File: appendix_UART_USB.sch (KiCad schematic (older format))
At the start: 27 parts, among them J504 USB_C_Receptacle, U502 FT2232D, X501 SG5032CCN-6.000000M-HJGA3

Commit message: fixed missing symbol issue fixed 3vout cap on FTDI
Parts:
- removed D501: USBLC6-2SC6, digikey-footprints:SOT23-6L, symbol dk_TVS-Diodes:USBLC6-2SC6
- added C1: 33n, Capacitors_SMD:C_0603, symbol Device:C
- added U1: USBLC6-2SC6, Package_TO_SOT_SMD:SOT-23-6, symbol Power_Protection:USBLC6-2SC6
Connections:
- net labels added: +3.3V, +5V
- net labels removed: 3.3V
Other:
- moved on the sheet: C501

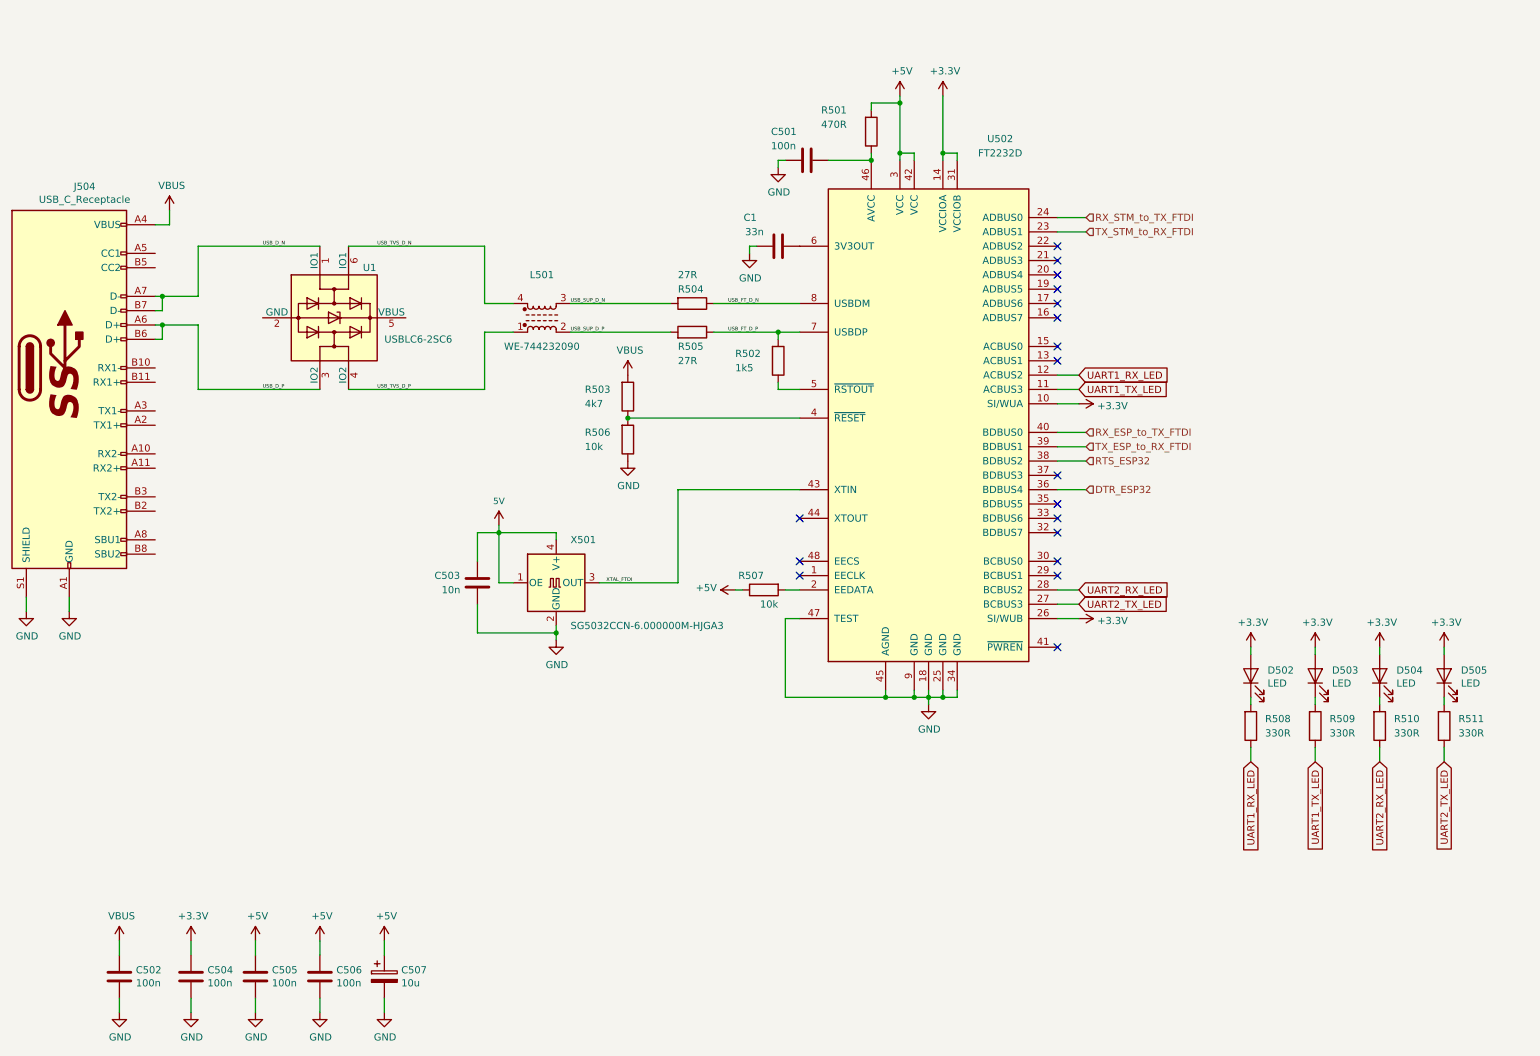
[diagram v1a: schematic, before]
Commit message: started with STM32 Pinout connections (Mittagspause)
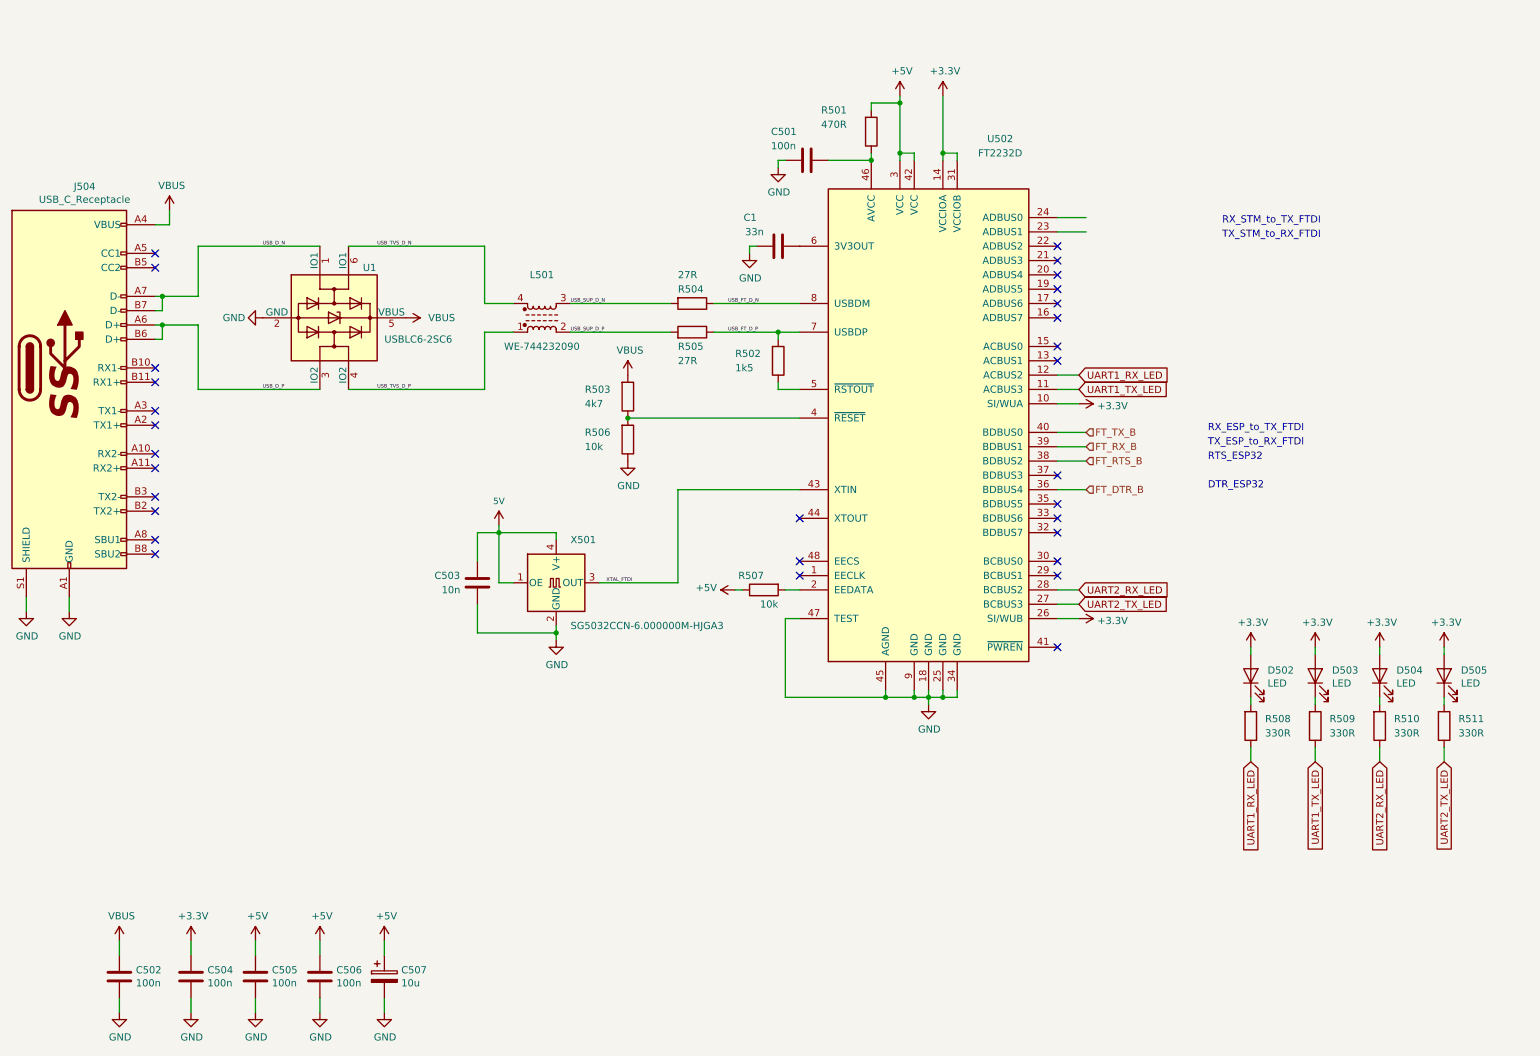
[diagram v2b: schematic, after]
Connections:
- net GND: now also U1.2 (GND)
- net VBUS: now also U1.5 (VBUS)
- net DTR_ESP32 renamed FT_DTR_B
- net RTS_ESP32 renamed FT_RTS_B
- net RX_ESP_to_TX_FTDI renamed FT_TX_B
- net RX_STM_to_TX_FTDI: no longer names the net of U502.24 (ADBUS0)
- net TX_ESP_to_RX_FTDI renamed FT_RX_B
- net TX_STM_to_RX_FTDI: no longer names the net of U502.23 (ADBUS1)
- no-connect marks 18 -> 30
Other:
- note added: "DTR_ESP32"
- note added: "RTS_ESP32"
- note added: "RX_ESP_to_TX_FTDI"
- note added: "RX_STM_to_TX_FTDI"
- note added: "TX_ESP_to_RX_FTDI"
- note added: "TX_STM_to_RX_FTDI"
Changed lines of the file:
@@
 $Descr A4 11693 8268
 encoding utf-8
-Sheet 5 6
+Sheet 6 6
 Title "USB to UART Interface"
 Date ""
@@
 Text Label 4850 4200 0    25   ~ 0
 XTAL_FTDI
-Text HLabel 8200 3150 2    50   Input ~ 0
-RX_ESP_to_TX_FTDI
-Text HLabel 8200 3250 2    50   Input ~ 0
-TX_ESP_to_RX_FTDI
-Text HLabel 8200 3550 2    50   Input ~ 0
-DTR_ESP32
-Text HLabel 8200 3350 2    50   Input ~ 0
-RTS_ESP32
 Wire Wire Line
 	8200 3550 8000 3550
@@
 Wire Wire Line
 	8000 3250 8200 3250
-Text HLabel 8200 1650 2    50   Input ~ 0
-RX_STM_to_TX_FTDI
-Text HLabel 8200 1750 2    50   Input ~ 0
-TX_STM_to_RX_FTDI
 Wire Wire Line
 	8200 1650 8000 1650
@@
 Wire Wire Line
 	5850 1850 5900 1850
+NoConn ~ 1700 4000
+NoConn ~ 1700 3900
+NoConn ~ 1700 3700
+NoConn ~ 1700 3600
+NoConn ~ 1700 3400
+NoConn ~ 1700 3300
+NoConn ~ 1700 3100
+NoConn ~ 1700 3000
+NoConn ~ 1700 2800
+NoConn ~ 1700 2700
+NoConn ~ 1700 2000
+NoConn ~ 1700 1900
+$Comp
+L power:VBUS #PWR0505
+U 1 1 5CC883C1
+P 3450 2350
+F 0 "#PWR0505" H 3450 2200 50  0001 C CNN
+F 1 "VBUS" V 3450 2600 50  0000 C CNN
+F 2 "" H 3450 2350 50  0001 C CNN
+F 3 "" H 3450 2350 50  0001 C CNN
+	1    3450 2350
+	0    1    1    0
+$EndComp
+$Comp
+L power:GND #PWR0504
+U 1 1 5CC897FA
+P 2450 2350
+F 0 "#PWR0504" H 2450 2100 50  0001 C CNN
+F 1 "GND" V 2450 2150 50  0000 C CNN
+F 2 "" H 2450 2350 50  0001 C CNN
+F 3 "" H 2450 2350 50  0001 C CNN
+	1    2450 2350
+	0    1    1    0
+$EndComp
+Text Notes 9150 1700 0    50   ~ 0
+RX_STM_to_TX_FTDI
+Text Notes 9150 1800 0    50   ~ 0
+TX_STM_to_RX_FTDI
+Text Notes 9050 3150 0    50   ~ 0
+RX_ESP_to_TX_FTDI
+Text Notes 9050 3250 0    50   ~ 0
+TX_ESP_to_RX_FTDI
+Text Notes 9050 3350 0    50   ~ 0
+RTS_ESP32
+Text Notes 9050 3550 0    50   ~ 0
+DTR_ESP32
+Text HLabel 8200 3250 2    50   Input ~ 0
+FT_RX_B
+Text HLabel 8200 3150 2    50   Input ~ 0
+FT_TX_B
+Text HLabel 8200 3550 2    50   Input ~ 0
+FT_DTR_B
+Text HLabel 8200 3350 2    50   Input ~ 0
+FT_RTS_B
 $EndSCHEMATC

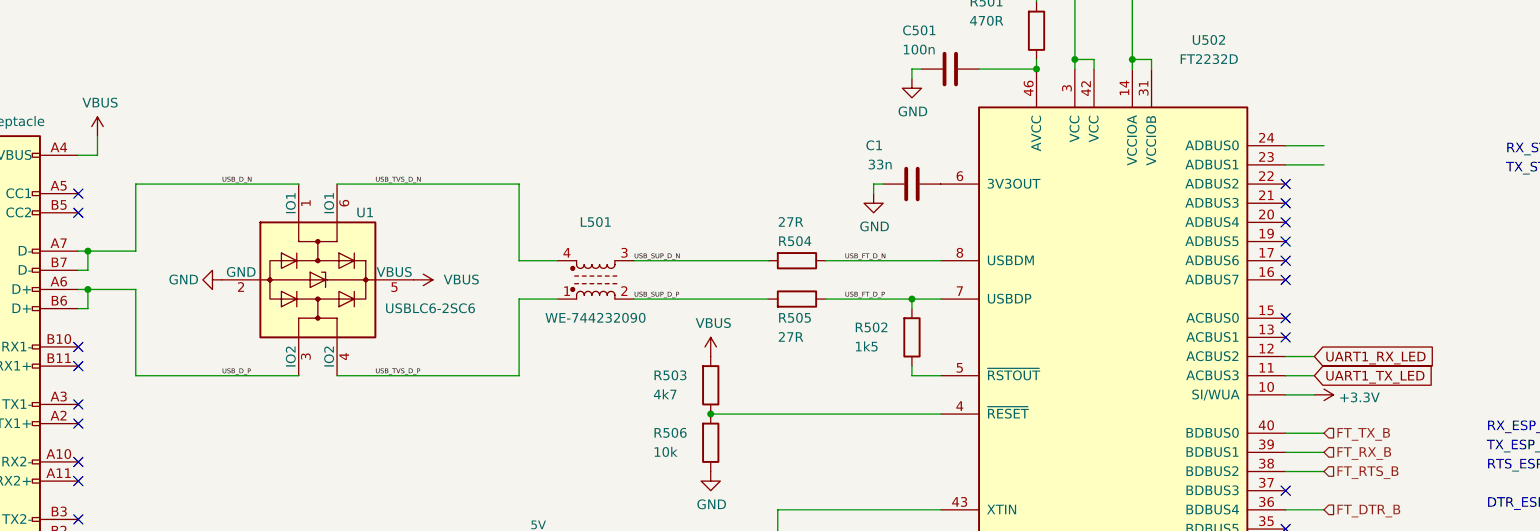
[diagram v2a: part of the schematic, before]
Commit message: layouted FT2232 / SD card
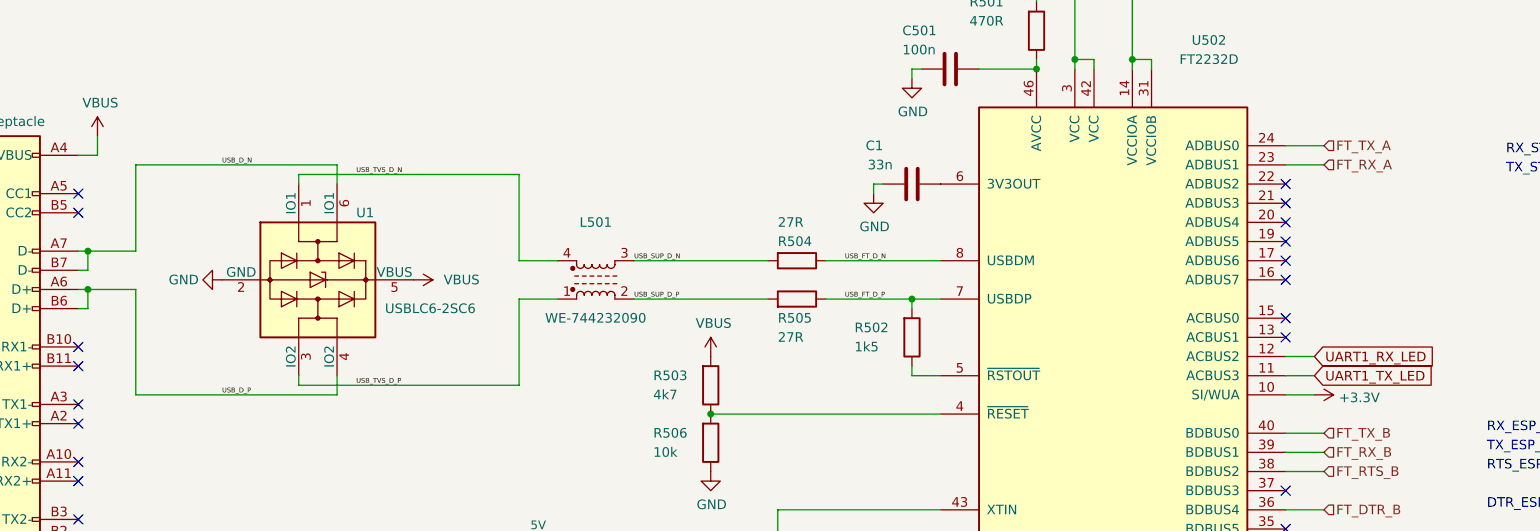
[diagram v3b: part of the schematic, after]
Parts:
- J504: footprint Connector_USB:USB_C_Receptacle_GCT_USB4085 -> Connectors_USB:USB_C_Receptacle_Amphenol_12401610E4-2A
- L501: footprint (none) -> FHNW-Pro4E-FS19T8-Library:WURTH_USB_Chocke_4PAD
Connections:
- net USB_D_N: now also U1.6 (IO1); no longer U1.1 (IO1)
- net USB_D_P: now also U1.4 (IO2); no longer U1.3 (IO2)
- net USB_TVS_D_N: now also U1.1 (IO1); no longer U1.6 (IO1)
- net USB_TVS_D_P: now also U1.3 (IO2); no longer U1.4 (IO2)
- net FT_RX_A: now reaches U502.23 (ADBUS1)
- net FT_TX_A: now reaches U502.24 (ADBUS0)
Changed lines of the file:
@@
 F 0 "J504" H 1207 3967 50  0000 C CNN
 F 1 "USB_C_Receptacle" H 1207 3876 50  0000 C CNN
-F 2 "Connector_USB:USB_C_Receptacle_GCT_USB4085" H 1250 2700 50  0001 C CNN
+F 2 "Connectors_USB:USB_C_Receptacle_Amphenol_12401610E4-2A" H 1250 2700 50  0001 C CNN
 F 3 "https://www.usb.org/sites/default/files/documents/usb_type-c.zip" H 1250 2700 50  0001 C CNN
 	1    1100 2700
@@
 Wire Wire Line
 	1750 2400 2000 2400
-Text Label 2450 2850 0    25   ~ 0
+Text Label 2450 2950 0    25   ~ 0
 USB_D_P
-Text Label 3250 2850 0    25   ~ 0
+Text Label 3150 2900 0    25   ~ 0
 USB_TVS_D_P
-Text Label 3250 1850 0    25   ~ 0
+Text Label 3150 1800 0    25   ~ 0
 USB_TVS_D_N
-Text Label 2450 1850 0    25   ~ 0
+Text Label 2450 1750 0    25   ~ 0
 USB_D_N
 $Comp
@@
 	1    5450 2450
 	0    1    -1   0
-$EndComp
-$Comp
-L FHNW-Pro4E-FS19T8-Library:WE-744232090 L501
-U 1 1 5CBA01CA
-P 4400 2350
-F 0 "L501" H 4400 2650 50  0000 C CNN
-F 1 "WE-744232090" H 4400 2150 50  0000 C CNN
-F 2 "" H 4400 2350 50  0001 C CNN
-F 3 "~" H 4400 2350 50  0001 C CNN
-	1    4400 2350
-	1    0    0    -1
 $EndComp
 Wire Wire Line
@@
 $EndComp
 $Comp
-L Power_Protection:USBLC6-2SC6 U1
-U 1 1 5CBD8D55
-P 2950 2350
-F 0 "U1" V 2600 2550 50  0000 L CNN
-F 1 "USBLC6-2SC6" V 3100 2700 50  0000 L CNN
-F 2 "Package_TO_SOT_SMD:SOT-23-6" H 2200 2750 50  0001 C CNN
-F 3 "http://www2.st.com/resource/en/datasheet/CD00050750.pdf" H 3150 2700 50  0001 C CNN
-	1    2950 2350
-	0    1    1    0
-$EndComp
-Wire Wire Line
-	2000 2400 2000 2850
-Wire Wire Line
-	2000 2850 2850 2850
-Wire Wire Line
-	2000 1850 2000 2200
-Wire Wire Line
-	2000 1850 2850 1850
-Wire Wire Line
-	4000 1850 4000 2250
-Wire Wire Line
-	3050 1850 4000 1850
-Wire Wire Line
-	4000 2450 4000 2850
-Wire Wire Line
-	3050 2850 4000 2850
-$Comp
 L Device:C C1
 U 1 1 5CBC7319
@@
 NoConn ~ 1700 2000
 NoConn ~ 1700 1900
-$Comp
-L power:VBUS #PWR0505
-U 1 1 5CC883C1
-P 3450 2350
-F 0 "#PWR0505" H 3450 2200 50  0001 C CNN
-F 1 "VBUS" V 3450 2600 50  0000 C CNN
-F 2 "" H 3450 2350 50  0001 C CNN
-F 3 "" H 3450 2350 50  0001 C CNN
-	1    3450 2350
-	0    1    1    0
-$EndComp
-$Comp
-L power:GND #PWR0504
-U 1 1 5CC897FA
-P 2450 2350
-F 0 "#PWR0504" H 2450 2100 50  0001 C CNN
-F 1 "GND" V 2450 2150 50  0000 C CNN
-F 2 "" H 2450 2350 50  0001 C CNN
-F 3 "" H 2450 2350 50  0001 C CNN
-	1    2450 2350
-	0    1    1    0
-$EndComp
 Text Notes 9150 1700 0    50   ~ 0
 RX_STM_to_TX_FTDI
@@
 Text HLabel 8200 3350 2    50   Input ~ 0
 FT_RTS_B
+$Comp
+L power:GND #PWR0504
+U 1 1 5CC897FA
+P 2450 2350
+F 0 "#PWR0504" H 2450 2100 50  0001 C CNN
+F 1 "GND" V 2450 2150 50  0000 C CNN
+F 2 "" H 2450 2350 50  0001 C CNN
+F 3 "" H 2450 2350 50  0001 C CNN
+	1    2450 2350
+	0    1    1    0
+$EndComp
+$Comp
+L power:VBUS #PWR0505
+U 1 1 5CC883C1
+P 3450 2350
+F 0 "#PWR0505" H 3450 2200 50  0001 C CNN
+F 1 "VBUS" V 3450 2600 50  0000 C CNN
+F 2 "" H 3450 2350 50  0001 C CNN
+F 3 "" H 3450 2350 50  0001 C CNN
+	1    3450 2350
+	0    1    1    0
+$EndComp
+$Comp
+L FHNW-Pro4E-FS19T8-Library:WE-744232090 L501
+U 1 1 5CBA01CA
+P 4400 2350
+F 0 "L501" H 4400 2650 50  0000 C CNN
+F 1 "WE-744232090" H 4400 2150 50  0000 C CNN
+F 2 "FHNW-Pro4E-FS19T8-Library:WURTH_USB_Chocke_4PAD" H 4400 2350 50  0001 C CNN
+F 3 "~" H 4400 2350 50  0001 C CNN
+	1    4400 2350
+	1    0    0    -1
+$EndComp
+Wire Wire Line
+	2000 2950 3050 2950
+Wire Wire Line
+	3050 2950 3050 2850
+Wire Wire Line
+	2000 2400 2000 2950
+Wire Wire Line
+	2850 2850 2850 2900
+Wire Wire Line
+	2850 2900 4000 2900
+Wire Wire Line
+	4000 2450 4000 2900
+$Comp
+L Power_Protection:USBLC6-2SC6 U1
+U 1 1 5CBD8D55
+P 2950 2350
+F 0 "U1" V 2600 2550 50  0000 L CNN
+F 1 "USBLC6-2SC6" V 3100 2700 50  0000 L CNN
+F 2 "Package_TO_SOT_SMD:SOT-23-6" H 2200 2750 50  0001 C CNN
+F 3 "http://www2.st.com/resource/en/datasheet/CD00050750.pdf" H 3150 2700 50  0001 C CNN
+	1    2950 2350
+	0    1    1    0
+$EndComp
+Wire Wire Line
+	2850 1850 2850 1800
+Wire Wire Line
+	2850 1800 4000 1800
+Wire Wire Line
+	4000 1800 4000 2250
+Wire Wire Line
+	3050 1850 3050 1750
+Wire Wire Line
+	3050 1750 2000 1750
+Wire Wire Line
+	2000 1750 2000 2200
+Text HLabel 8200 1750 2    50   Input ~ 0
+FT_RX_A
+Text HLabel 8200 1650 2    50   Input ~ 0
+FT_TX_A
 $EndSCHEMATC
